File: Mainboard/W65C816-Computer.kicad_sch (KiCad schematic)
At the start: 31 parts, among them J1 ADDR_DATA_DBG, J2 CTRL_BANK_DBG, J3 CPU_MISC_DBG, SW1 RESET, U1 W65C816S6PG-14, U2 SN74AHC373N, U3 SN74AHC14N, X1 ECS-P143X-8.000-BN

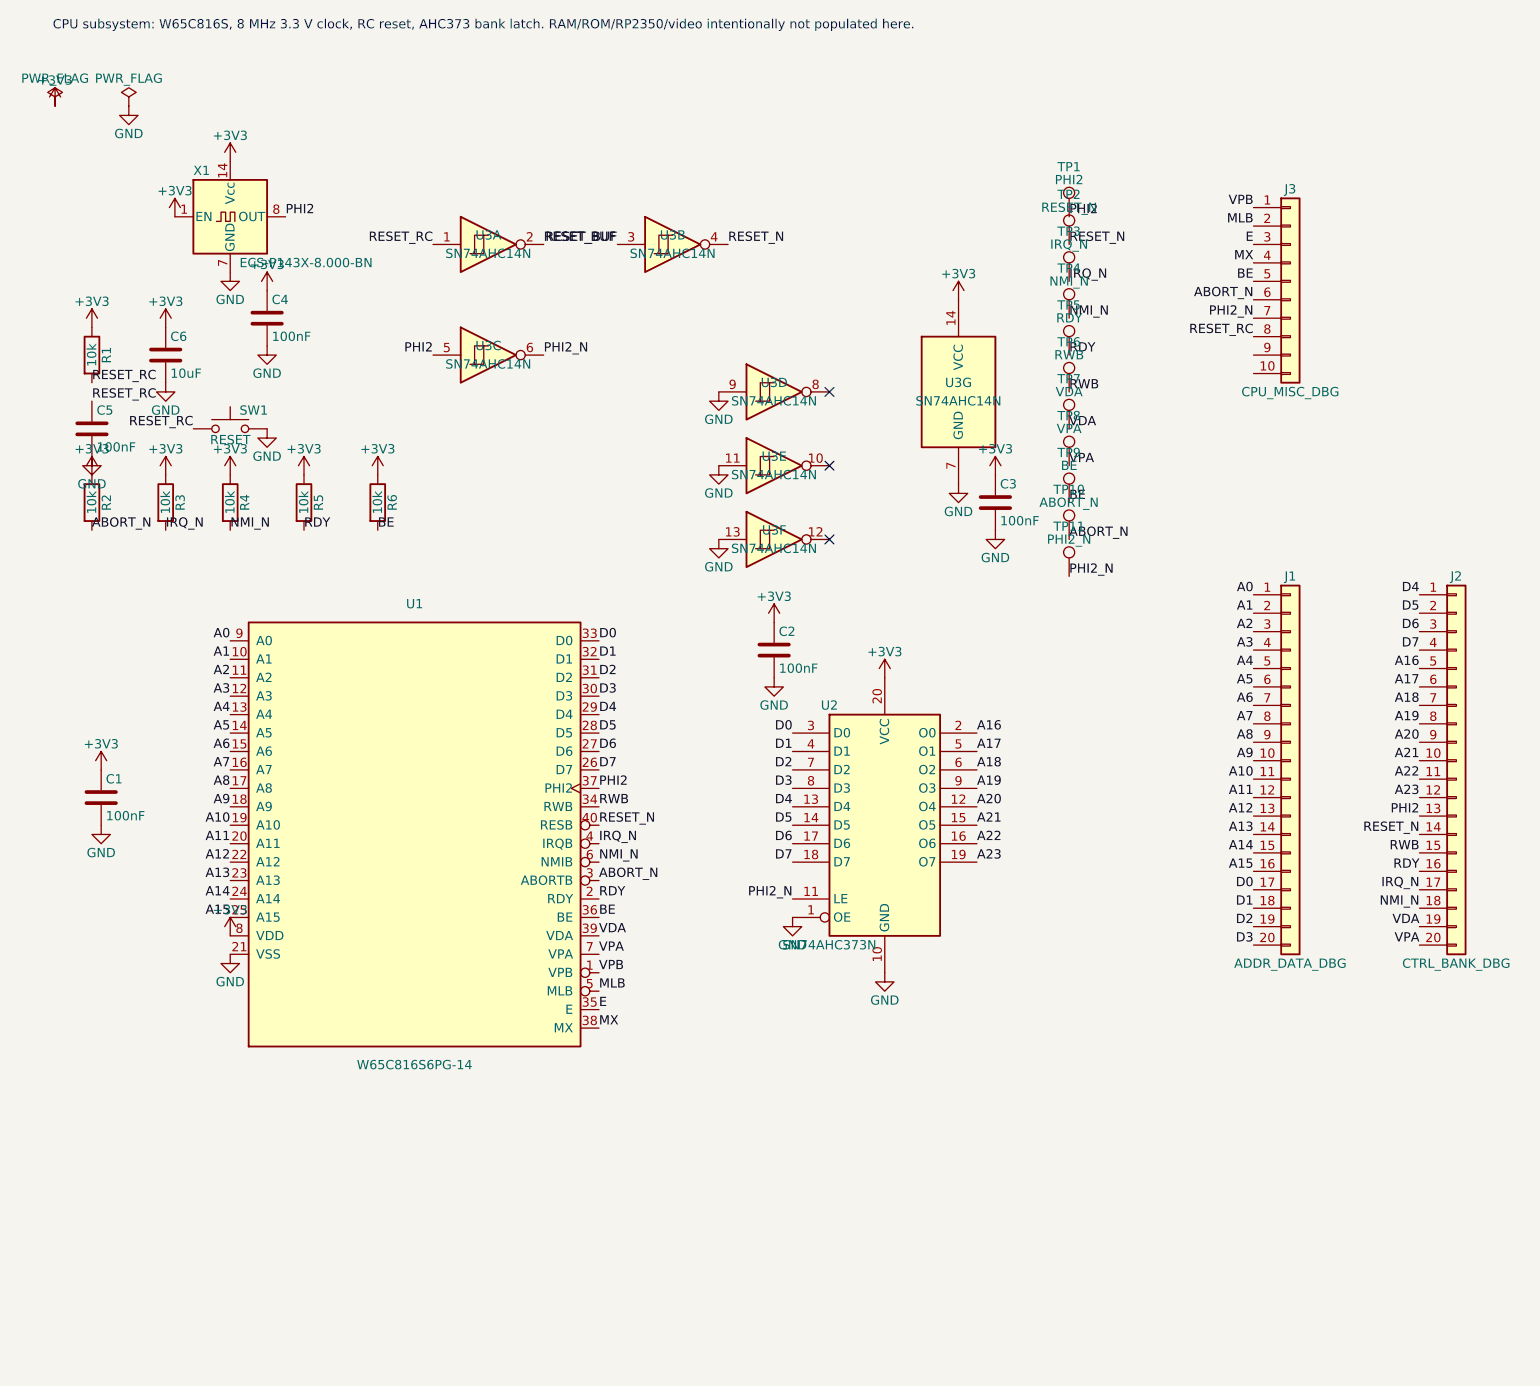
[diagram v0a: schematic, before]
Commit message: Add symbol library and lock file for W65C816-Computer project
- Created a new symbol library table for the W65C816-Computer project.
- Added a lock file to manage project access on the local machine.
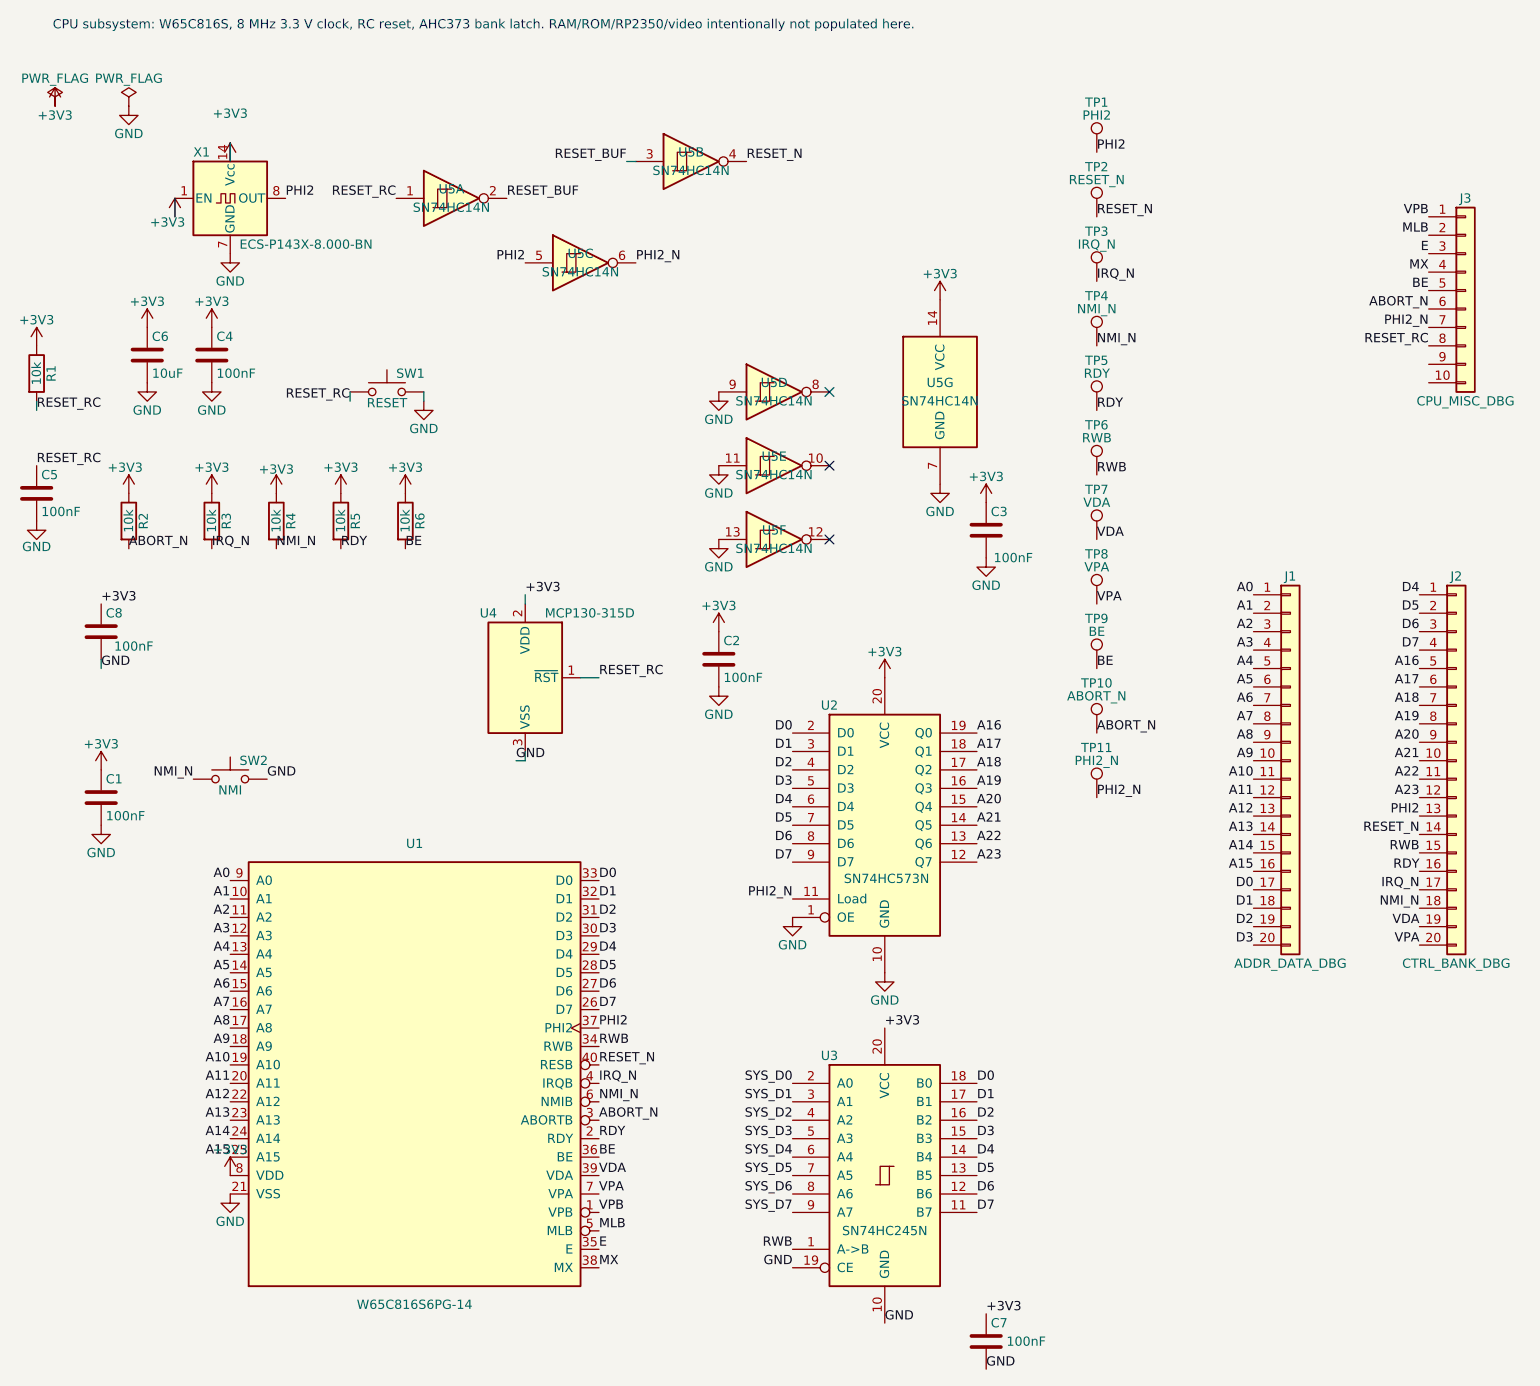
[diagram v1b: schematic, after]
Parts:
- added C7, C8: 100nF, Capacitor_THT:C_Disc_D3.0mm_W1.6mm_P2.50mm, symbol Device:C
- added SW2: NMI, Button_Switch_THT:SW_PUSH_6mm_H4.3mm, symbol Switch:SW_Push
- added U3: SN74HC245N, Package_DIP:DIP-20_W7.62mm_Socket_LongPads, symbol 74xx:74HC245
- added U4: MCP130-315D, Package_TO_SOT_THT:TO-92_Inline, symbol Power_Supervisor:MCP130-xxxDxTO
- U2: value SN74AHC373N -> SN74HC573N; symbol 74xx:74AHC373 -> 74xx:74LS573
- U5: renamed from U3; value SN74AHC14N -> SN74HC14N
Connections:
- net +3V3: now also C7.1, C8.1, U3.20 (VCC), U4.2 (VDD)
- net A16: now also U2.19 (Q0); no longer U2.2 (O0)
- net A17: now also U2.18 (Q1); no longer U2.5 (O1)
- net A18: now also U2.17 (Q2); no longer U2.6 (O2)
- net A19: now also U2.16 (Q3); no longer U2.9 (O3)
- net A20: now also U2.15 (Q4); no longer U2.12 (O4)
- net A21: now also U2.14 (Q5); no longer U2.15 (O5)
- net A22: now also U2.13 (Q6); no longer U2.16 (O6)
- net A23: now also U2.12 (Q7); no longer U2.19 (O7)
- net D0: now also U2.2 (D0), U3.18 (B0); no longer U2.3 (D0)
- net D1: now also U2.3 (D1), U3.17 (B1); no longer U2.4 (D1)
- net D2: now also U2.4 (D2), U3.16 (B2); no longer U2.7 (D2)
- net D3: now also U2.5 (D3), U3.15 (B3); no longer U2.8 (D3)
- net D4: now also U2.6 (D4), U3.14 (B4); no longer U2.13 (D4)
- net D5: now also U2.7 (D5), U3.13 (B5); no longer U2.14 (D5)
- net D6: now also U2.8 (D6), U3.12 (B6); no longer U2.17 (D6)
- net D7: now also U2.9 (D7), U3.11 (B7); no longer U2.18 (D7)
- net GND: now also C7.2, C8.2, SW2.2, U3.10 (GND), U3.19 (CE), U4.3 (VSS)
- net NMI_N: now also SW2.1
- net RESET_RC: now also U4.1 (~{RST})
- net RWB: now also U3.1 (A->B)
- new net SYS_D0: U3.2 (A0)
- new net SYS_D1: U3.3 (A1)
- new net SYS_D2: U3.4 (A2)
- new net SYS_D3: U3.5 (A3)
- new net SYS_D4: U3.6 (A4)
- new net SYS_D5: U3.7 (A5)
- new net SYS_D6: U3.8 (A6)
- new net SYS_D7: U3.9 (A7)
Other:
- moved on the sheet: C2, C3, C4, C5, C6, J3, R1, R2, R3, R4, R5, R6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

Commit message: Refactor code structure for improved readability and maintainability
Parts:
- added C10, C11, C12, C20, C30, C41, C43, C9: 100nF, Capacitor_THT:C_Disc_D3.0mm_W1.6mm_P2.50mm, symbol Device:C
- added C40, C42: 470uF, Capacitor_THT:CP_Radial_D8.0mm_P5.00mm, symbol Device:C_Polarized
- added D1: P6KE5.0A, Diode_THT:D_DO-15_P10.16mm_Horizontal, symbol Device:D_TVS
- added F1: 2.5A, Fuse:Fuseholder_Clip-5x20mm_Littelfuse_111_Inline_P20.00x5.00mm_D1.05mm_Horizontal, symbol Device:Fuse
- added J4: PJ-102A 5V_IN, PJ-102A:CUI_PJ-102A, symbol PJ-102A:PJ-102A
- added J5: DAUGHTER_PWR_AUX, Connector_PinSocket_2.54mm:PinSocket_1x06_P2.54mm_Vertical, symbol Connector_Generic:Conn_01x06
- added JP1: FLASH_WE_EN, Connector_PinHeader_2.54mm:PinHeader_1x02_P2.54mm_Vertical, symbol Connector_Generic:Conn_01x02
- added LED1: PWR, LED_THT:LED_D5.0mm, symbol Device:LED
- added MOD1: 3V3_BUCK_MODULE_5V_IN_3A, Connector_PinSocket_2.54mm:PinSocket_1x04_P2.54mm_Vertical, symbol Connector_Generic:Conn_01x04
- added Q1: P-MOSFET_REV_PROT_TO220, Package_TO_SOT_THT:TO-220-3_Vertical, symbol Transistor_FET:Q_PMOS_GDS
- added R30: 10k, Resistor_THT:R_Axial_DIN0207_L6.3mm_D2.5mm_P7.62mm_Horizontal, symbol Device:R
- added R41: 1k, Resistor_THT:R_Axial_DIN0207_L6.3mm_D2.5mm_P7.62mm_Horizontal, symbol Device:R
- added SW3: MAIN_PWR_SW_EXT, TerminalBlock_RND:TerminalBlock_RND_205-00232_1x02_P5.08mm_Horizontal, symbol Switch:SW_SPST
- added TP12: RAM_CS0_N, TestPoint:TestPoint_THTPad_D1.5mm_Drill0.7mm, symbol Connector:TestPoint
- added TP13: RAM_CS1_N, TestPoint:TestPoint_THTPad_D1.5mm_Drill0.7mm, symbol Connector:TestPoint
- added TP14: RAM_CS2_N, TestPoint:TestPoint_THTPad_D1.5mm_Drill0.7mm, symbol Connector:TestPoint
- added TP15: RAM_CS3_N, TestPoint:TestPoint_THTPad_D1.5mm_Drill0.7mm, symbol Connector:TestPoint
- added TP16: RAM_CS4_N, TestPoint:TestPoint_THTPad_D1.5mm_Drill0.7mm, symbol Connector:TestPoint
- added TP17: RAM_CS5_N, TestPoint:TestPoint_THTPad_D1.5mm_Drill0.7mm, symbol Connector:TestPoint
- added TP18: RAM_CS6_N, TestPoint:TestPoint_THTPad_D1.5mm_Drill0.7mm, symbol Connector:TestPoint
- added TP19: RAM_CS7_N, TestPoint:TestPoint_THTPad_D1.5mm_Drill0.7mm, symbol Connector:TestPoint
- added TP20: ROM_CS_N, TestPoint:TestPoint_THTPad_D1.5mm_Drill0.7mm, symbol Connector:TestPoint
- added TP21: MEM_OE_N, TestPoint:TestPoint_THTPad_D1.5mm_Drill0.7mm, symbol Connector:TestPoint
- added TP22: MEM_WE_N, TestPoint:TestPoint_THTPad_D1.5mm_Drill0.7mm, symbol Connector:TestPoint
- added TP23: +5V, TestPoint:TestPoint_THTPad_D1.5mm_Drill0.7mm, symbol Connector:TestPoint
- added TP24: +3V3, TestPoint:TestPoint_THTPad_D1.5mm_Drill0.7mm, symbol Connector:TestPoint
- added TP25: GND, TestPoint:TestPoint_THTPad_D1.5mm_Drill0.7mm, symbol Connector:TestPoint
- added U10: SN74HC04N, Package_DIP:DIP-14_W7.62mm_Socket_LongPads, symbol 74xx:74HC04
- added U20: AS6C4008-55PCN, Package_DIP:DIP-32_W15.24mm_Socket_LongPads, symbol Memory_RAM:AS6C4008-55PCN
- added U30: SST39VF040-70-4I-NHE, Package_LCC:PLCC-32_THT-Socket, symbol Memory_Flash:SST39SF040
- added U6, U7: SN74HC138N, Package_DIP:DIP-16_W7.62mm_Socket_LongPads, symbol 74xx:74HC138
- added U9: SN74HC00N, Package_DIP:DIP-14_W7.62mm_Socket_LongPads, symbol 74xx:74HC00
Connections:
- net +3V3: now also C10.1, C11.1, C12.1, C20.1, C30.1, C42.1, C43.1, C9.1, J5.3 (Pin_3), MOD1.3 (Pin_3), R30.2, TP24.1, U10.14 (VCC), U20.32 (VCC), U30.32 (VCC), U6.16 (VCC), U6.6 (E2), U7.16 (VCC), U7.6 (E2), U9.14 (VCC)
- net A0: now also U20.12 (A0), U30.12 (A0)
- net A1: now also U20.11 (A1), U30.11 (A1)
- net A10: now also U20.23 (A10), U30.23 (A10)
- net A11: now also U20.25 (A11), U30.25 (A11)
- net A12: now also U20.4 (A12), U30.4 (A12)
- net A13: now also U20.28 (A13), U30.28 (A13)
- net A14: now also U20.3 (A14), U30.29 (A14)
- net A15: now also U20.31 (A15), U30.3 (A15), U9.2
- net A16: now also U20.2 (A16), U30.2 (A16), U6.1 (A0)
- net A17: now also U20.30 (A17), U30.30 (A17), U6.2 (A1)
- net A18: now also U20.1 (A18), U30.1 (A18), U6.3 (A2)
- net A19: now also U7.1 (A0)
- net A2: now also U20.10 (A2), U30.10 (A2)
- net A20: now also U7.2 (A1)
- net A21: now also U7.3 (A2)
- net A22: now also U7.4 (~{E0})
- net A23: now also U7.5 (~{E1})
- net A3: now also U20.9 (A3), U30.9 (A3)
- net A4: now also U20.8 (A4), U30.8 (A4)
- net A5: now also U20.7 (A5), U30.7 (A5)
- net A6: now also U20.6 (A6), U30.6 (A6)
- net A7: now also U20.5 (A7), U30.5 (A7)
- net A8: now also U20.27 (A8), U30.27 (A8)
- net A9: now also U20.26 (A9), U30.26 (A9)
- net GND: now also C10.2, C11.2, C12.2, C20.2, C30.2, C40.2, C41.2, C42.2, C43.2, C9.2, D1.2 (A2), J4.2, J5.4 (Pin_4), J5.5 (Pin_5), J5.6 (Pin_6), LED1.1 (K), MOD1.2 (Pin_2), MOD1.4 (Pin_4), Q1.1 (G), TP25.1, U10.11, U10.13, U10.7 (GND), U20.16 (VSS), U30.16 (GND), U6.5 (~{E1}), U6.8 (GND), U7.8 (GND), U9.10, U9.12, U9.13, U9.7 (GND), U9.9
- net RWB: now also U10.5
- net SYS_D0: now also U20.13 (DQ0), U30.13 (D0)
- net SYS_D1: now also U20.14 (DQ1), U30.14 (D1)
- net SYS_D2: now also U20.15 (DQ2), U30.15 (D2)
- net SYS_D3: now also U20.17 (DQ3), U30.17 (D3)
- net SYS_D4: now also U20.18 (DQ4), U30.18 (D4)
- net SYS_D5: now also U20.19 (DQ5), U30.19 (D5)
- net SYS_D6: now also U20.20 (DQ6), U30.20 (D6)
- net SYS_D7: now also U20.21 (DQ7), U30.21 (D7)
- new net +5V: C40.1, C41.1, D1.1 (A1), J5.1 (Pin_1), J5.2 (Pin_2), MOD1.1 (Pin_1), Q1.3 (S), R41.1, TP23.1
- new net +5V_FUSED: F1.2, SW3.1 (A)
- new net +5V_IN: F1.1, J4.1
- new net +5V_SW: Q1.2 (D), SW3.2 (B)
- new net BANK00: U10.2, U9.1
- new net BANK00_N: U10.1, U6.15 (~{Y0})
- new net MEM_OE_N: TP21.1, U10.6, U10.9, U20.24 (OE#), U30.24 (OE)
- new net MEM_WE_N: JP1.2 (Pin_2), TP22.1, U10.8, U20.29 (WE#)
- new net PWR_LED_A: LED1.2 (A), R41.2
- new net RAM_BLOCK0: U10.4, U9.4
- new net RAM_BLOCK0_N: U10.3, U6.4 (~{E0}), U7.15 (~{Y0})
- new net RAM_CS0_N: TP12.1, U20.22 (CE#), U9.6
- new net RAM_CS1_N: TP13.1, U7.14 (~{Y1})
- new net RAM_CS2_N: TP14.1, U7.13 (~{Y2})
- new net RAM_CS3_N: TP15.1, U7.12 (~{Y3})
- new net RAM_CS4_N: TP16.1, U7.11 (~{Y4})
- new net RAM_CS5_N: TP17.1, U7.10 (~{Y5})
- new net RAM_CS6_N: TP18.1, U7.9 (~{Y6})
- new net RAM_CS7_N: TP19.1, U7.7 (~{Y7})
- new net ROM_CS_N: TP20.1, U30.22 (CE), U9.3, U9.5
- new net ROM_WE_N: JP1.1 (Pin_1), R30.1, U30.31 (PGM)
- no-connect marks 3 -> 17
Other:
- note added: "Power input: PJ-102A barrel jack is center-positive and rated 2.5 A. +5V is fused, switched, reverse-polarity protected by Q1, TVS-clamped, then feeds the daughterboard power connector and MOD1 3.3 V buck module."
- note added: "Rev A decode: U7 divides low 4 MB into 512 KB SRAM banks; U6 detects bank $00. Flash overlays $00:8000-$FFFF for reset vectors. U9 disables RAM0 while ROM is active. MEM_OE_N=!RWB, MEM_WE_N=RWB."
- note added: "Stage 1 subsystem: W65C816S, 8 MHz 3.3 V clock, MCP130 reset, 74HC573 bank latch, one AS6C4008 SRAM, SST39VF040 boot Flash. RP2350/video not populated here."
- note removed: "CPU subsystem: W65C816S, 8 MHz 3.3 V clock, RC reset, AHC373 bank latch. RAM/ROM/RP2350/video intentionally not populated here."
- moved on the sheet: J1, J2, J3
